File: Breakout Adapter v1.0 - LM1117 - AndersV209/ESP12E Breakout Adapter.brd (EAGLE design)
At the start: 27.5 x 38.8 mm, 10 parts, among them IC1 LM1117-3.3

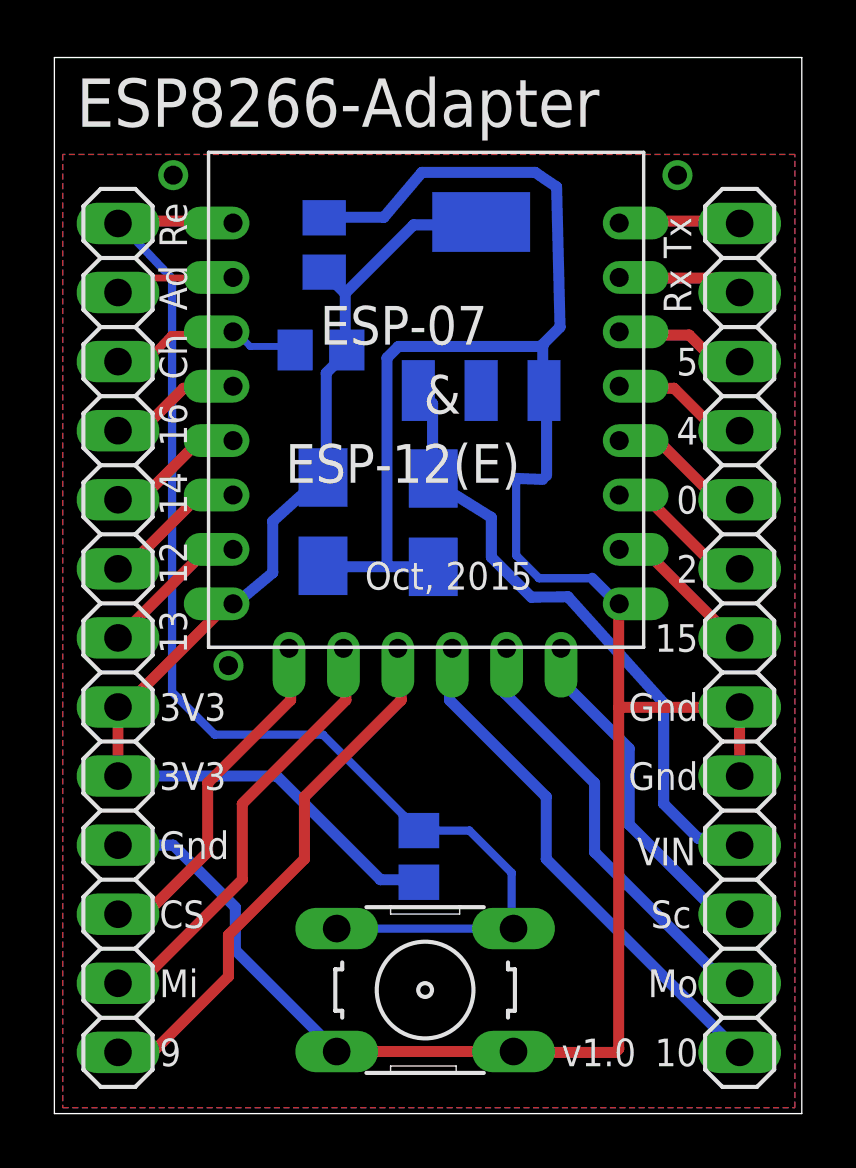
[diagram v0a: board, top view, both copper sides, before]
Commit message: repostiton of esp12e
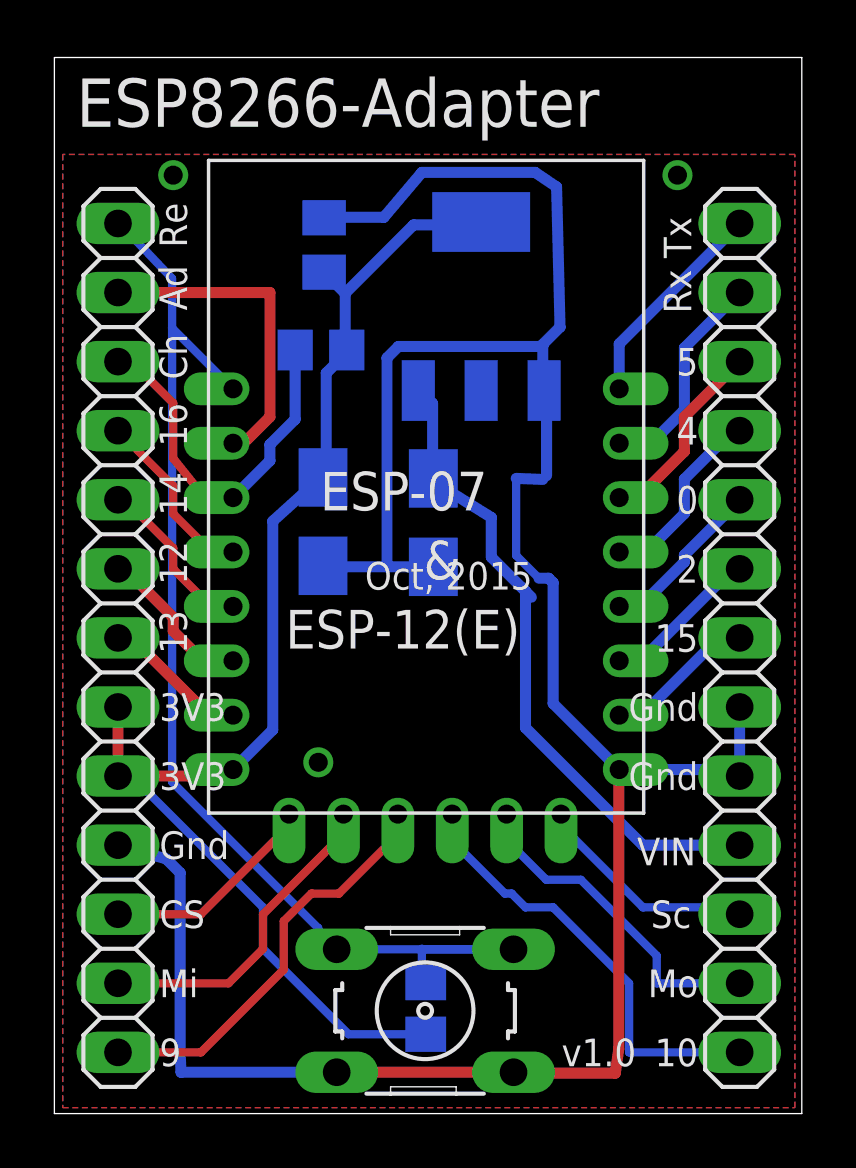
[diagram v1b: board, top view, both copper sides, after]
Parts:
- moved ESP8266 6.10 mm to (15.7, 23.7)
- moved R2 5.59 mm to (15.6, 6.70)
- moved RESET_SWITCH 0.76 mm to (15.6, 6.61)
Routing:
- net VCC: track 42.3 -> 50.1 mm
- net ADC: track 4.60 -> 11.9 mm
- net CH_PD: track 7.41 -> 13.9 mm
- net CS0: track 13.0 -> 8.07 mm
- net SCLK: track 13.0 -> 8.34 mm
- net GPIO9: track 20.0 -> 15.4 mm
- net MISO: track 16.3 -> 12.0 mm
- net MOSI: track 16.2 -> 12.3 mm
- net RX: track 4.69 -> 8.06 mm
- net TX: track 4.55 -> 7.92 mm
- net GPIO10: track 19.3 -> 16.3 mm
- net GND: track 93.4 -> 96.1 mm
- net GPIO5: track 4.97 -> 7.25 mm
- net RESET: track 46.3 -> 44.4 mm
- net GPIO4: track 5.16 -> 7.02 mm
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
